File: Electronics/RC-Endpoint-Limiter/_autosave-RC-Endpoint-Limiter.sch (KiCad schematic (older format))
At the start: 54 parts, among them J1 USB_B_Micro, J10 ISCP, J2 Hall Low, J3 Hall High, J4 Switch Low, J5 Switch High, J6 RC Input, J7 RC Output, J8 Inhibit Input, J9 I2C header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

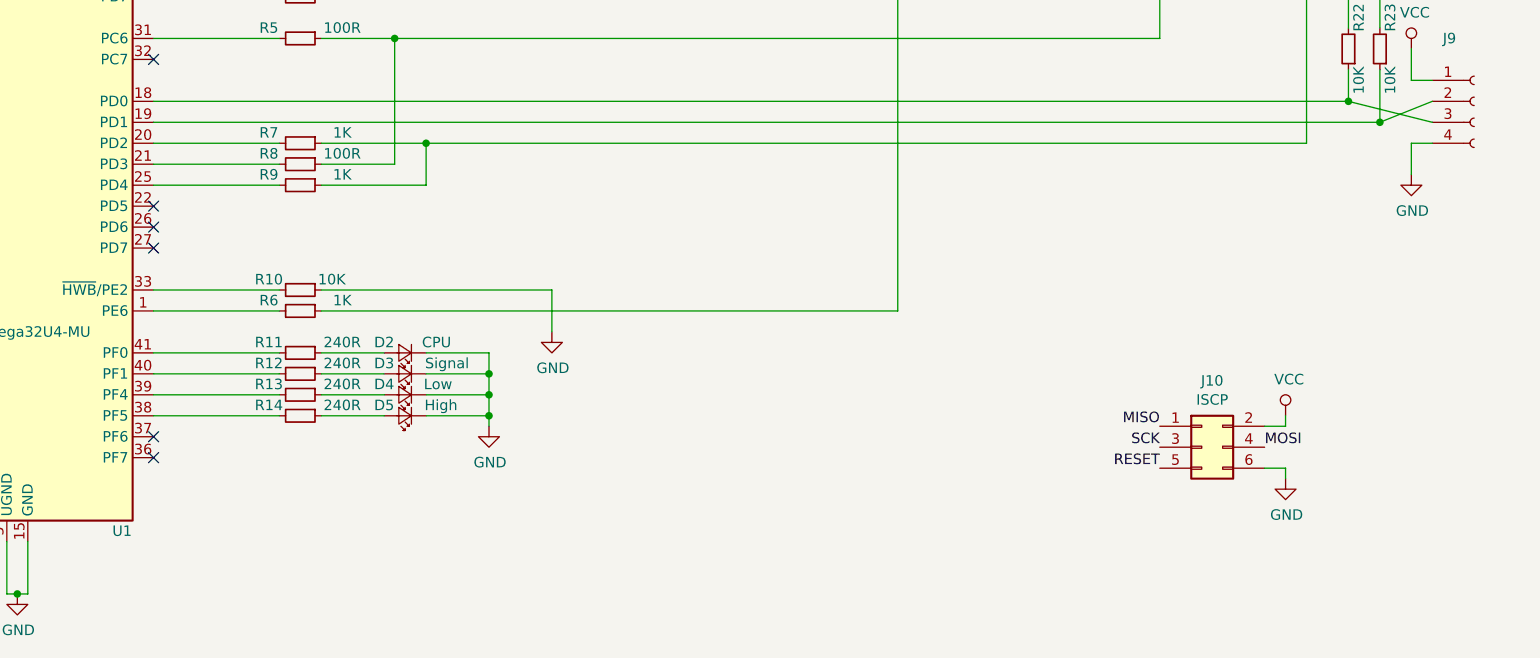
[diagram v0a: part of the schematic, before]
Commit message: added lots more I/O
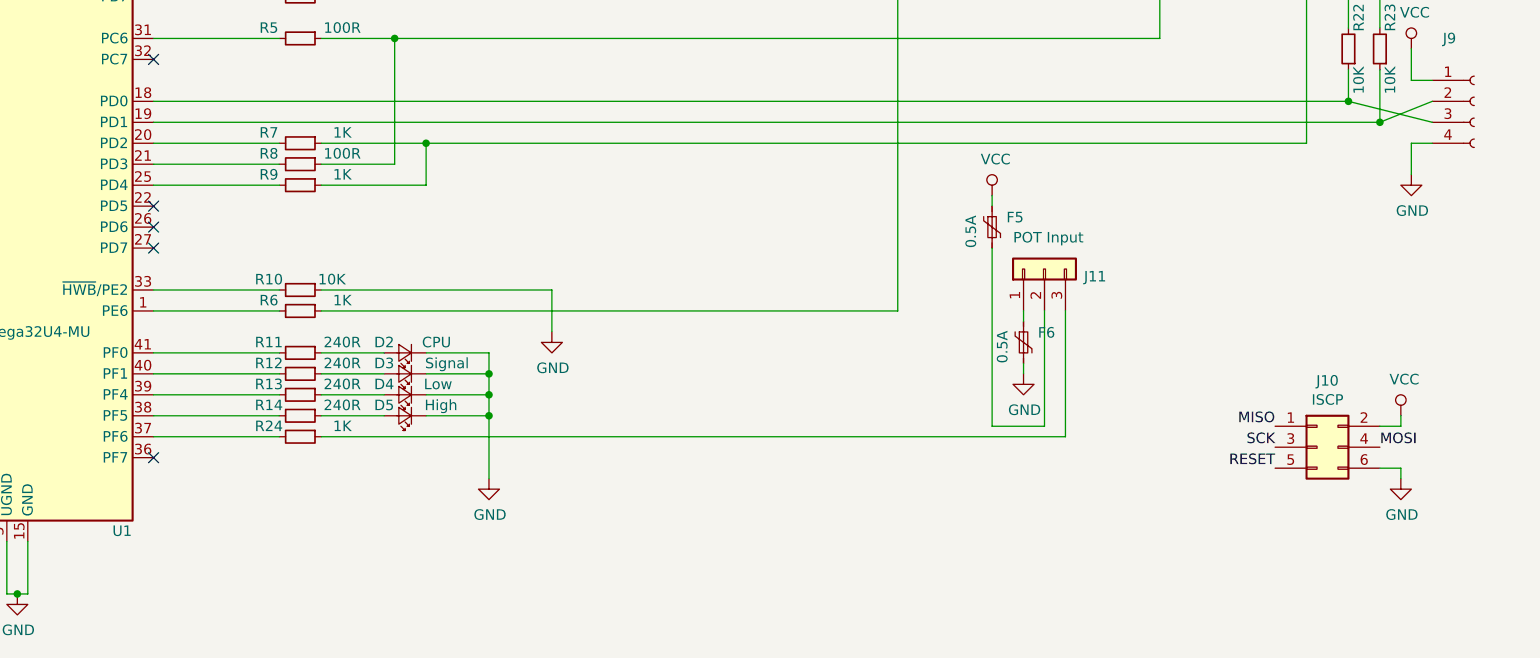
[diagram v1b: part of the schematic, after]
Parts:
- added F5, F6: 0.5A, Fuse:Fuse_0603_1608Metric, symbol Device:Polyfuse_Small
- added J11: POT Input, Connector_PinHeader_1.27mm:PinHeader_1x03_P1.27mm_Horizontal, symbol Connector_Generic:Conn_01x03
- added R24: 1K, Resistor_SMD:R_0603_1608Metric, symbol Device:R_Small
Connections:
- net GND: now also F6.2
- net VCC: now also F5.1
- net at U1.37 (PF6): now also R24.2
- new net: F6.1, J11.1 (Pin_1)
- new net: F5.2, J11.2 (Pin_2)
- new net: J11.3 (Pin_3), R24.1
- no-connect marks 9 -> 8
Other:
- moved on the sheet: J10
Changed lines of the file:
@@
 L power:GND #PWR014
 U 1 1 5D6BA7FA
-P 6450 5650
-F 0 "#PWR014" H 6450 5400 50  0001 C CNN
-F 1 "GND" H 6455 5477 50  0000 C CNN
-F 2 "" H 6450 5650 50  0001 C CNN
-F 3 "" H 6450 5650 50  0001 C CNN
-	1    6450 5650
-	1    0    0    -1
-$EndComp
-Wire Wire Line
-	6450 5600 6450 5650
+P 6450 5900
+F 0 "#PWR014" H 6450 5650 50  0001 C CNN
+F 1 "GND" H 6455 5727 50  0000 C CNN
+F 2 "" H 6450 5900 50  0001 C CNN
+F 3 "" H 6450 5900 50  0001 C CNN
+	1    6450 5900
+	1    0    0    -1
+$EndComp
 Wire Wire Line
 	6450 5500 6450 5600
@@
 NoConn ~ 4850 4700
 NoConn ~ 4850 4800
-NoConn ~ 4850 5700
 NoConn ~ 4850 5800
 Wire Wire Line
@@
 L Connector_Generic:Conn_02x03_Odd_Even J10
 U 1 1 5D9485AA
-P 9850 5750
-F 0 "J10" H 9900 6067 50  0000 C CNN
-F 1 "ISCP" H 9900 5976 50  0000 C CNN
-F 2 "Connector_PinHeader_1.27mm:PinHeader_2x03_P1.27mm_Vertical" H 9850 5750 50  0001 C CNN
-F 3 "~" H 9850 5750 50  0001 C CNN
-	1    9850 5750
+P 10400 5750
+F 0 "J10" H 10450 6067 50  0000 C CNN
+F 1 "ISCP" H 10450 5976 50  0000 C CNN
+F 2 "Connector_PinHeader_1.27mm:PinHeader_2x03_P1.27mm_Vertical" H 10400 5750 50  0001 C CNN
+F 3 "~" H 10400 5750 50  0001 C CNN
+	1    10400 5750
 	1    0    0    -1
 $EndComp
@@
 Text Label 4850 3100 0    50   ~ 0
 MOSI
-Text Label 9650 5650 2    50   ~ 0
+Text Label 10200 5650 2    50   ~ 0
 MISO
 $Comp
 L power:VCC #PWR0105
 U 1 1 5D99ACF3
-P 10250 5600
-F 0 "#PWR0105" H 10250 5450 50  0001 C CNN
-F 1 "VCC" H 10267 5773 50  0000 C CNN
-F 2 "" H 10250 5600 50  0001 C CNN
-F 3 "" H 10250 5600 50  0001 C CNN
-	1    10250 5600
-	1    0    0    -1
-$EndComp
-Wire Wire Line
-	10150 5650 10250 5650
-Wire Wire Line
-	10250 5650 10250 5600
-Text Label 9650 5750 2    50   ~ 0
+P 10800 5600
+F 0 "#PWR0105" H 10800 5450 50  0001 C CNN
+F 1 "VCC" H 10817 5773 50  0000 C CNN
+F 2 "" H 10800 5600 50  0001 C CNN
+F 3 "" H 10800 5600 50  0001 C CNN
+	1    10800 5600
+	1    0    0    -1
+$EndComp
+Wire Wire Line
+	10700 5650 10800 5650
+Wire Wire Line
+	10800 5650 10800 5600
+Text Label 10200 5750 2    50   ~ 0
 SCK
-Text Label 9650 5850 2    50   ~ 0
+Text Label 10200 5850 2    50   ~ 0
 RESET
-Text Label 10150 5750 0    50   ~ 0
+Text Label 10700 5750 0    50   ~ 0
 MOSI
 $Comp
 L power:GND #PWR0106
 U 1 1 5D9A30F9
-P 10250 5900
-F 0 "#PWR0106" H 10250 5650 50  0001 C CNN
-F 1 "GND" H 10255 5727 50  0000 C CNN
-F 2 "" H 10250 5900 50  0001 C CNN
-F 3 "" H 10250 5900 50  0001 C CNN
-	1    10250 5900
-	1    0    0    -1
-$EndComp
-Wire Wire Line
-	10150 5850 10250 5850
-Wire Wire Line
-	10250 5850 10250 5900
+P 10800 5900
+F 0 "#PWR0106" H 10800 5650 50  0001 C CNN
+F 1 "GND" H 10805 5727 50  0000 C CNN
+F 2 "" H 10800 5900 50  0001 C CNN
+F 3 "" H 10800 5900 50  0001 C CNN
+	1    10800 5900
+	1    0    0    -1
+$EndComp
+Wire Wire Line
+	10700 5850 10800 5850
+Wire Wire Line
+	10800 5850 10800 5900
 Text Label 4850 3200 0    50   ~ 0
 MISO
@@
 Wire Wire Line
 	6400 2000 6400 3200
+$Comp
+L Connector_Generic:Conn_01x03 J11
+U 1 1 5DA5C445
+P 9100 4900
+F 0 "J11" V 9064 4712 50  0000 R CNN
+F 1 "POT Input" V 9250 5050 50  0000 R CNN
+F 2 "Connector_PinHeader_1.27mm:PinHeader_1x03_P1.27mm_Horizontal" H 9100 4900 50  0001 C CNN
+F 3 "~" H 9100 4900 50  0001 C CNN
+	1    9100 4900
+	0    -1   -1   0
+$EndComp
+$Comp
+L power:VCC #PWR0107
+U 1 1 5DA5C44B
+P 8850 4550
+F 0 "#PWR0107" H 8850 4400 50  0001 C CNN
+F 1 "VCC" H 8867 4723 50  0000 C CNN
+F 2 "" H 8850 4550 50  0001 C CNN
+F 3 "" H 8850 4550 50  0001 C CNN
+	1    8850 4550
+	1    0    0    -1
+$EndComp
+$Comp
+L power:GND #PWR0108
+U 1 1 5DA5C451
+P 9000 5400
+F 0 "#PWR0108" H 9000 5150 50  0001 C CNN
+F 1 "GND" H 9005 5227 50  0000 C CNN
+F 2 "" H 9000 5400 50  0001 C CNN
+F 3 "" H 9000 5400 50  0001 C CNN
+	1    9000 5400
+	1    0    0    -1
+$EndComp
+$Comp
+L Device:Polyfuse_Small F6
+U 1 1 5DA5C459
+P 9000 5250
+F 0 "F6" H 9068 5296 50  0000 L CNN
+F 1 "0.5A" V 8900 5150 50  0000 L CNN
+F 2 "Fuse:Fuse_0603_1608Metric" H 9050 5050 50  0001 L CNN
+F 3 "~" H 9000 5250 50  0001 C CNN
+	1    9000 5250
+	1    0    0    -1
+$EndComp
+Wire Wire Line
+	9000 5150 9000 5100
+Wire Wire Line
+	9000 5350 9000 5400
+$Comp
+L Device:Polyfuse_Small F5
+U 1 1 5DA5C461
+P 8850 4700
+F 0 "F5" H 8918 4746 50  0000 L CNN
+F 1 "0.5A" V 8750 4600 50  0000 L CNN
+F 2 "Fuse:Fuse_0603_1608Metric" H 8900 4500 50  0001 L CNN
+F 3 "~" H 8850 4700 50  0001 C CNN
+	1    8850 4700
+	1    0    0    -1
+$EndComp
+Wire Wire Line
+	8850 5650 9100 5650
+Wire Wire Line
+	9100 5650 9100 5100
+Wire Wire Line
+	8850 5650 8850 4800
+Wire Wire Line
+	6450 5600 6450 5900
+Wire Wire Line
+	4850 5700 5450 5700
+Wire Wire Line
+	9200 5700 9200 5100
+Wire Wire Line
+	8850 4550 8850 4600
+$Comp
+L Device:R_Small R24
+U 1 1 5DAC9E36
+P 5550 5700
+F 0 "R24" V 5500 5550 50  0000 C CNN
+F 1 "1K" V 5500 5900 50  0000 C CNN
+F 2 "Resistor_SMD:R_0603_1608Metric" H 5550 5700 50  0001 C CNN
+F 3 "~" H 5550 5700 50  0001 C CNN
+	1    5550 5700
+	0    1    1    0
+$EndComp
+Wire Wire Line
+	5650 5700 9200 5700
 $EndSCHEMATC
